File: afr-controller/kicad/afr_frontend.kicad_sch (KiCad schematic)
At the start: 37 parts, among them J1 LSU_4.9, J2 MCU_IF, Q1 VND14NV04, U1 MCP6004, U3 REF3033, U5 AD8628

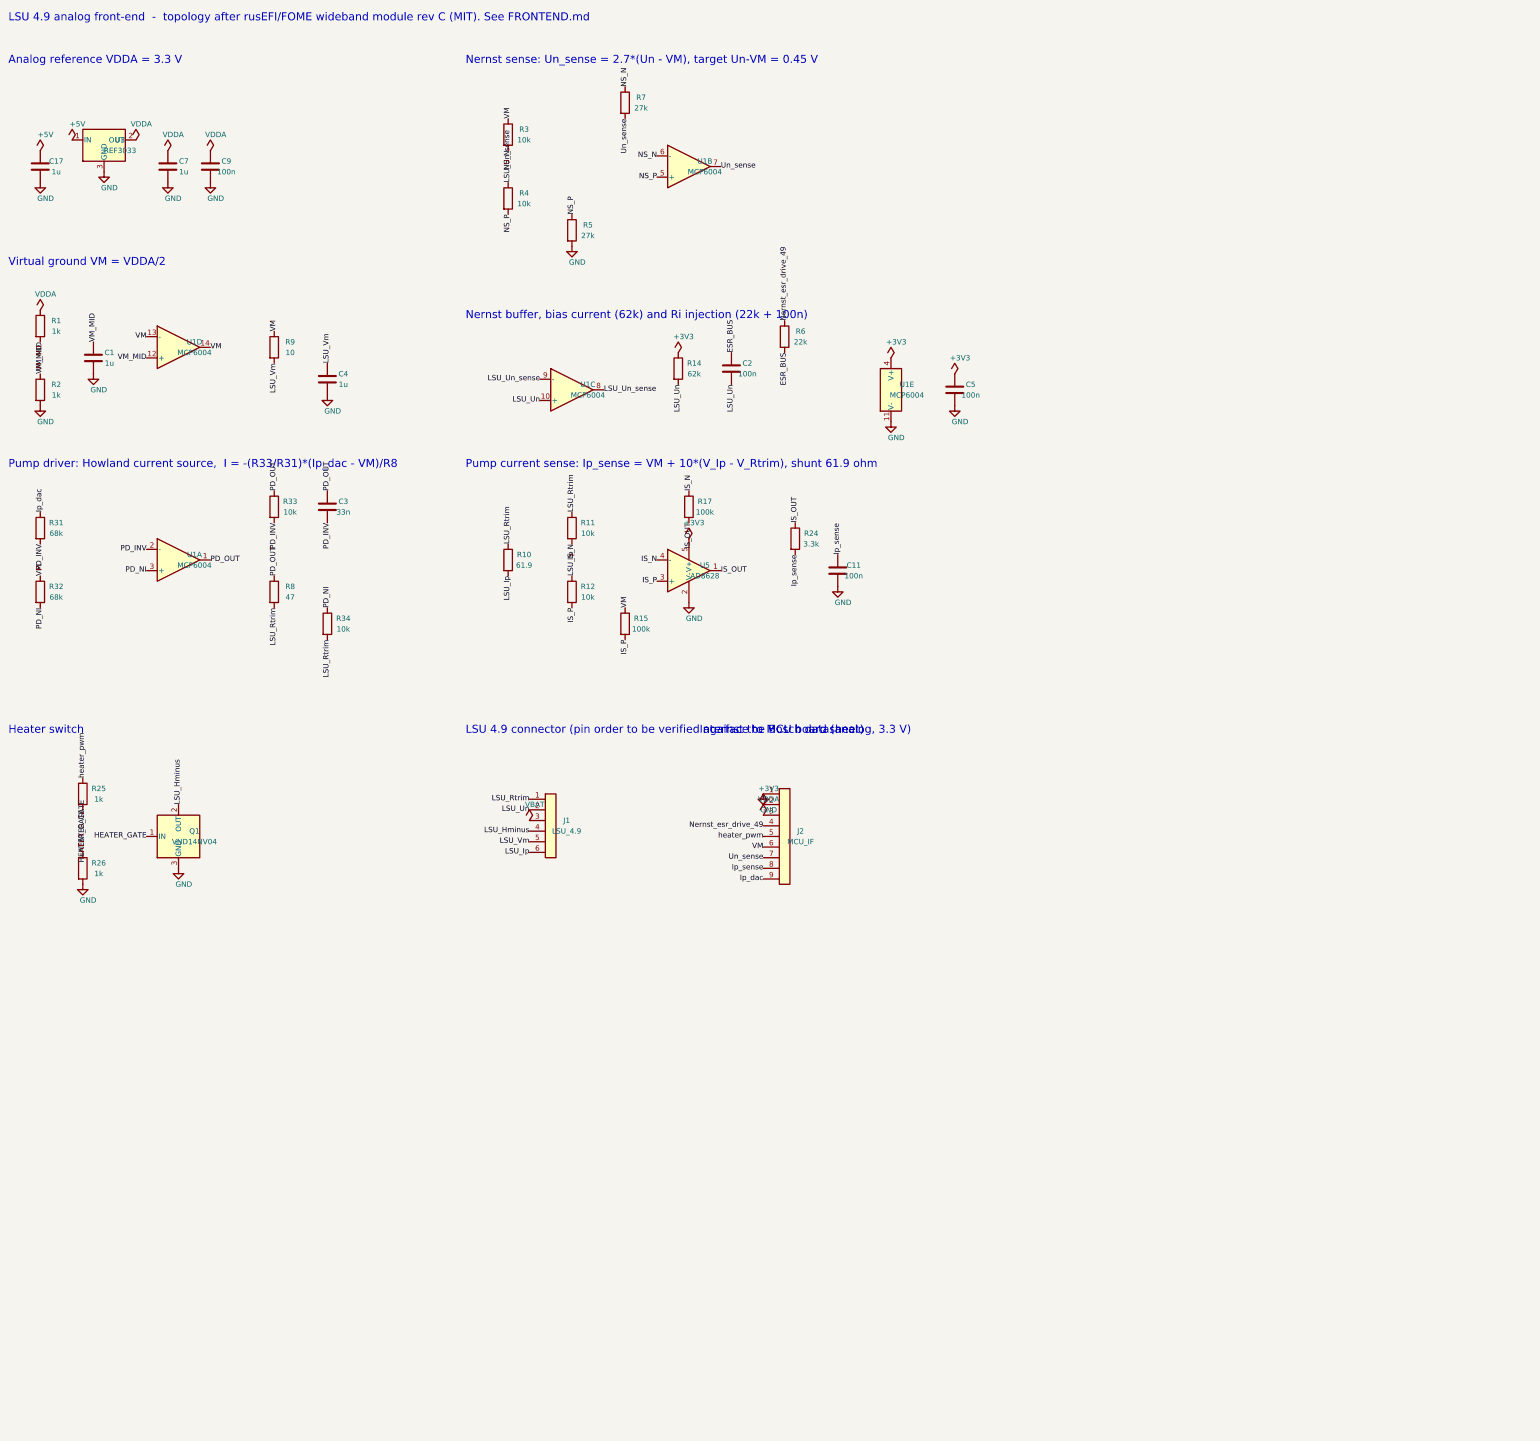
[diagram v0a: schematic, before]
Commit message: Add power, CAN and 0-5 V output to schematic generator, netlist check against kicad-cli, preview PDF
Co-Authored-By: Claude Sonnet 5.5 <noreply@anthropic.com>
Claude-Session: https://claude.ai/code/session_01RFGsein5uGNQp2jtJno8vX
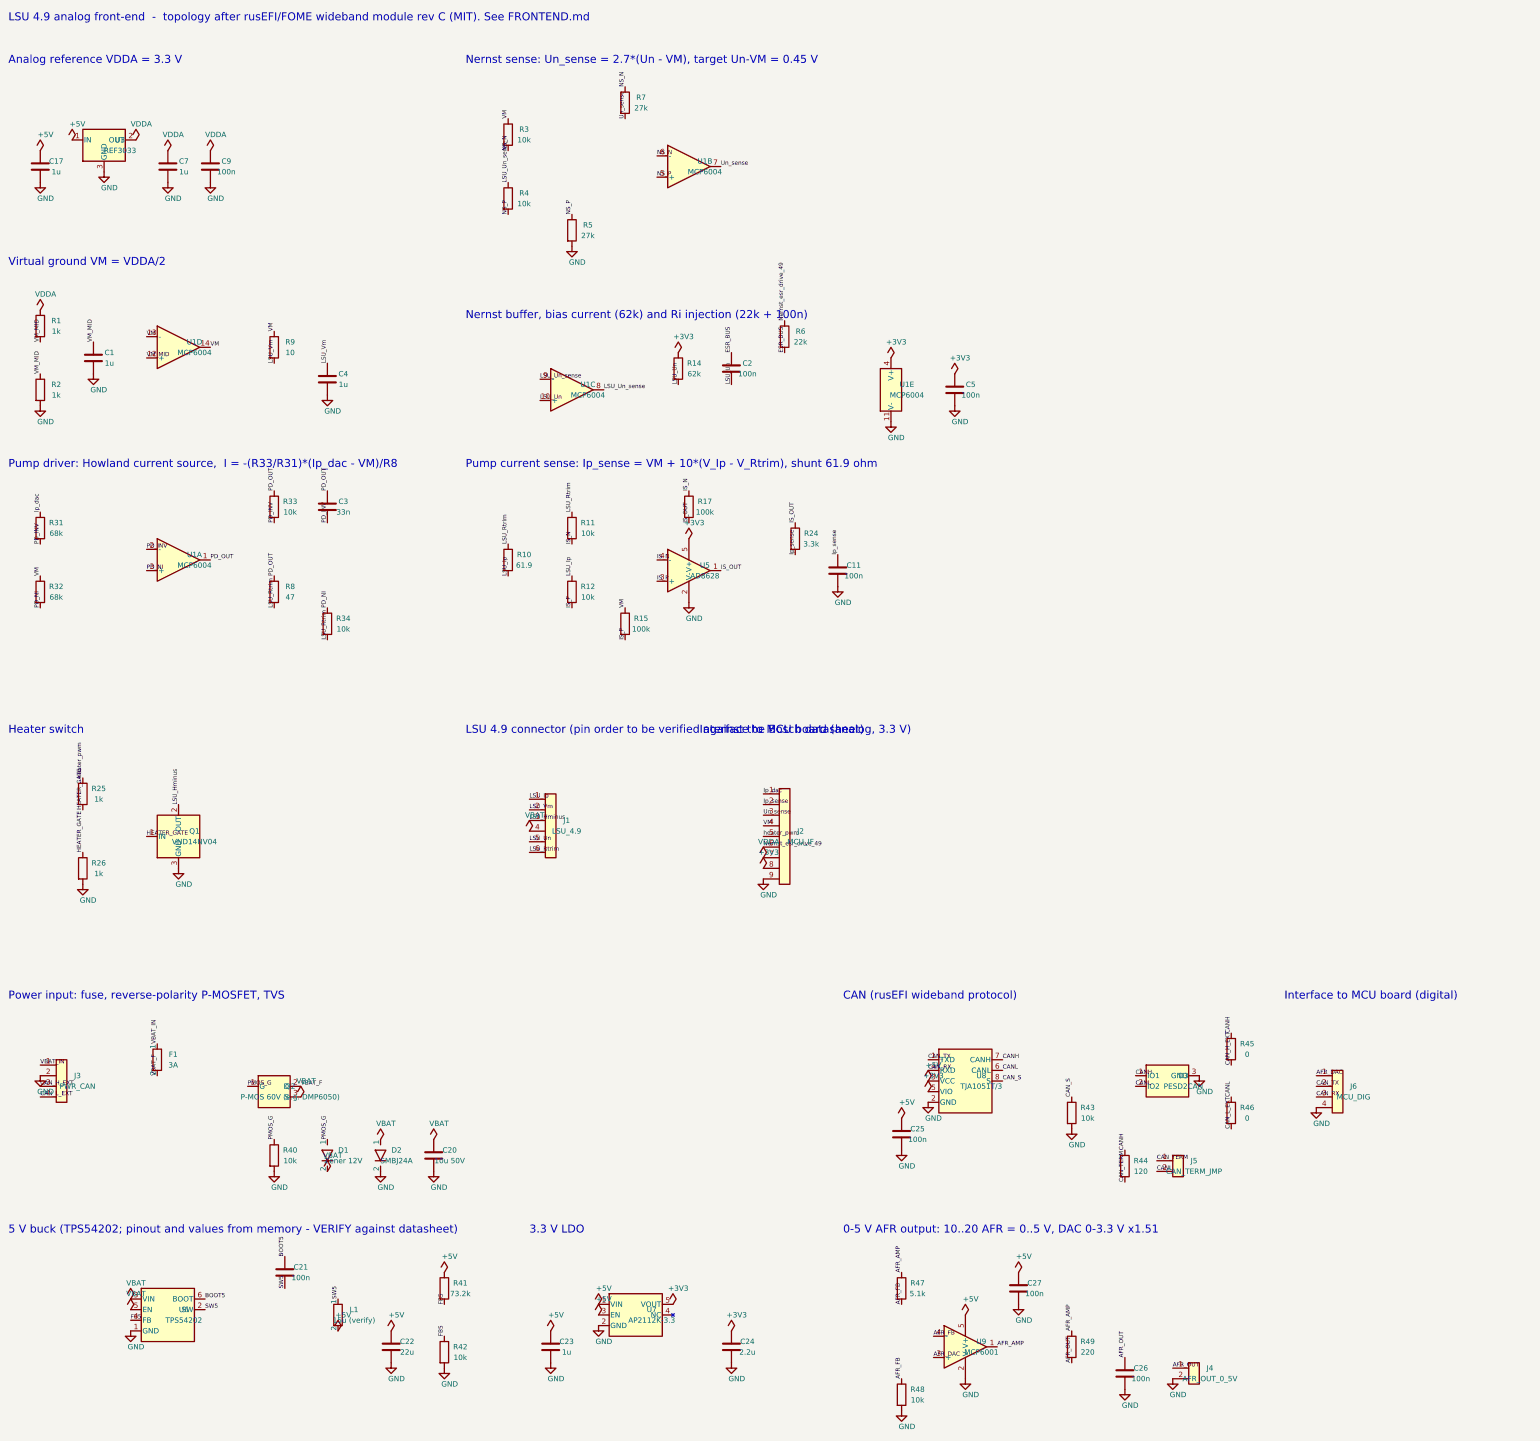
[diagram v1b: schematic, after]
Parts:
- added C20: 10u 50V, Capacitor_SMD:C_1206_3216Metric, symbol Local:C
- added C21, C25, C26, C27: 100n, Capacitor_SMD:C_0603_1608Metric, symbol Local:C
- added C22: 22u, Capacitor_SMD:C_1206_3216Metric, symbol Local:C
- added C23: 1u, Capacitor_SMD:C_0603_1608Metric, symbol Local:C
- added C24: 2.2u, Capacitor_SMD:C_0603_1608Metric, symbol Local:C
- added D1: Zener 12V, Diode_SMD:D_SOD-323, symbol Local:D
- added D2: SMBJ24A, Diode_SMD:D_SMB, symbol Local:D
- added D3: PESD2CAN, Package_TO_SOT_SMD:SOT-23, symbol Local:PESD2CAN
- added F1: 3A, Fuse:Fuse_1206_3216Metric, symbol Local:Fuse
- added J3: PWR_CAN, Connector_Molex:Molex_Micro-Fit_3.0_43650-0400, symbol Local:Conn_01x04
- added J4: AFR_OUT_0_5V, Connector_Molex:Molex_Micro-Fit_3.0_43650-0200, symbol Local:Conn_01x02
- added J5: CAN_TERM_JMP, Connector_PinHeader_2.54mm:PinHeader_1x02_P2.54mm_Vertical, symbol Local:Conn_01x02
- added J6: MCU_DIG, Connector_PinHeader_2.54mm:PinHeader_1x04_P2.54mm_Vertical, symbol Local:Conn_01x04
- added L1: 15u (verify), Inductor_SMD:L_Bourns_SRN6045, symbol Local:L
- added Q2: P-MOS 60V (e.g. DMP6050), Package_TO_SOT_SMD:SOT-23, symbol Local:Q_PMOS
- added R40, R42, R43, R48: 10k, Resistor_SMD:R_0603_1608Metric, symbol Local:R
- added R41: 73.2k, Resistor_SMD:R_0603_1608Metric, symbol Local:R
- added R44: 120, Resistor_SMD:R_0603_1608Metric, symbol Local:R
- added R45, R46: 0, Resistor_SMD:R_0603_1608Metric, symbol Local:R
- added R47: 5.1k, Resistor_SMD:R_0603_1608Metric, symbol Local:R
- added R49: 220, Resistor_SMD:R_0603_1608Metric, symbol Local:R
- added U6: TPS54202, Package_TO_SOT_SMD:SOT-23-6, symbol Local:TPS54202
- added U7: AP2112K-3.3, Package_TO_SOT_SMD:SOT-23-5, symbol Local:AP2112K-3.3
- added U8: TJA1051T/3, Package_SO:SOIC-8_3.9x4.9mm_P1.27mm, symbol Local:TJA1051T-3
- added U9: MCP6001, Package_TO_SOT_SMD:SOT-23-5, symbol Local:OPAMP5
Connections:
- net +3V3: now also J2.8 (Pin_8), C24.1, U7.5 (VOUT), U8.5 (VIO); no longer J2.2 (Pin_2)
- net +5V: now also C22.1, C23.1, C25.1, C27.1, L1.2, R41.1, U7.1 (VIN), U7.3 (EN), U8.3 (VCC), U9.5 (V+)
- net GND: now also J2.9 (Pin_9), C20.2, C22.2, C23.2, C24.2, C25.2, C26.2, C27.2, D2.2, D3.3 (GND), J3.2 (Pin_2), J4.2 (Pin_2), J6.4 (Pin_4), R40.2, R42.2, R43.2, R48.2, U6.1 (GND), U7.2 (GND), U8.2 (GND), U9.2 (V-); no longer J2.1 (Pin_1)
- net Ip_dac: now also J2.1 (Pin_1); no longer J2.9 (Pin_9)
- net Ip_sense: now also J2.2 (Pin_2); no longer J2.8 (Pin_8)
- net LSU_Hminus: now also J1.3 (Pin_3); no longer J1.4 (Pin_4)
- net LSU_Ip: now also J1.1 (Pin_1); no longer J1.6 (Pin_6)
- net LSU_Rtrim: now also J1.6 (Pin_6); no longer J1.1 (Pin_1)
- net LSU_Un: now also J1.5 (Pin_5); no longer J1.2 (Pin_2)
- net LSU_Vm: now also J1.2 (Pin_2); no longer J1.5 (Pin_5)
- net Nernst_esr_drive_49: now also J2.6 (Pin_6); no longer J2.4 (Pin_4)
- net Un_sense: now also J2.3 (Pin_3); no longer J2.7 (Pin_7)
- net VBAT: now also J1.4 (Pin_4), C20.1, D1.2, D2.1, Q2.3 (S), U6.3 (VIN), U6.5 (EN); no longer J1.3 (Pin_3)
- net VDDA: now also J2.7 (Pin_7); no longer J2.3 (Pin_3)
- net VM: now also J2.4 (Pin_4); no longer J2.6 (Pin_6)
- new net AFR_AMP: R47.1, R49.1, U9.1
- new net AFR_DAC: J6.1 (Pin_1), U9.3 (+)
- new net AFR_FB: R47.2, R48.1, U9.4 (-)
- new net AFR_OUT: C26.1, J4.1 (Pin_1), R49.2
- new net BOOT5: C21.1, U6.6 (BOOT)
- new net CANH: D3.1 (IO1), R44.1, R45.1, U8.7 (CANH)
- new net CANL: D3.2 (IO2), J5.2 (Pin_2), R46.1, U8.6 (CANL)
- new net CAN_H_EXT: J3.3 (Pin_3), R45.2
- new net CAN_L_EXT: J3.4 (Pin_4), R46.2
- new net CAN_RX: J6.3 (Pin_3), U8.4 (RXD)
- new net CAN_S: R43.1, U8.8 (S)
- new net CAN_TERM: J5.1 (Pin_1), R44.2
- new net CAN_TX: J6.2 (Pin_2), U8.1 (TXD)
- new net FB5: R41.2, R42.1, U6.4 (FB)
- new net PMOS_G: D1.1, Q2.1 (G), R40.1
- new net SW5: C21.2, L1.1, U6.2 (SW)
- new net VBAT_F: F1.2, Q2.2 (D)
- new net VBAT_IN: F1.1, J3.1 (Pin_1)
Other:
- note added: "0-5 V AFR output: 10..20 AFR = 0..5 V, DAC 0-3.3 V x1.51"
- note added: "3.3 V LDO"
- note added: "5 V buck (TPS54202; pinout and values from memory - VERIFY against datasheet)"
- note added: "CAN (rusEFI wideband protocol)"
- note added: "Interface to MCU board (digital)"
- note added: "Power input: fuse, reverse-polarity P-MOSFET, TVS"

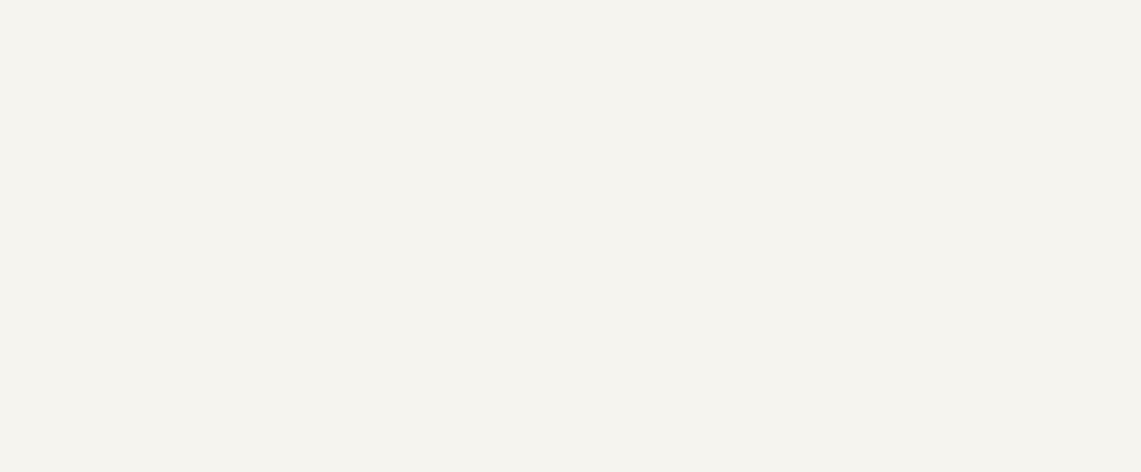
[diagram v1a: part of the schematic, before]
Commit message: Fix ERC: add PWR_FLAGs and local symbol library table
Co-Authored-By: Claude Sonnet 5.5 <noreply@anthropic.com>
Claude-Session: https://claude.ai/code/session_01RFGsein5uGNQp2jtJno8vX
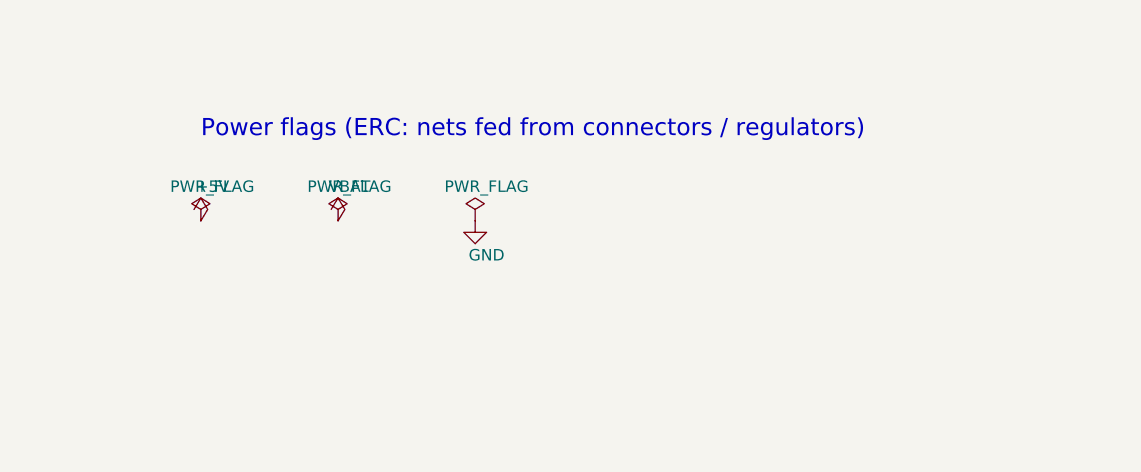
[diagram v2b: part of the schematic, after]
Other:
- note added: "Power flags (ERC: nets fed from connectors / regulators)"

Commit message: Fix footprint names, diode pin convention and P-MOS pinout; add footprint check
Co-Authored-By: Claude Sonnet 5.5 <noreply@anthropic.com>
Claude-Session: https://claude.ai/code/session_01RFGsein5uGNQp2jtJno8vX
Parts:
- J1: footprint Connector_Molex:Molex_Micro-Fit_3.0_43650-0600 -> Connector_Molex:Molex_Micro-Fit_3.0_43650-0600_1x06_P3.00mm_Horizontal
- J3: footprint Connector_Molex:Molex_Micro-Fit_3.0_43650-0400 -> Connector_Molex:Molex_Micro-Fit_3.0_43650-0400_1x04_P3.00mm_Horizontal
- J4: footprint Connector_Molex:Molex_Micro-Fit_3.0_43650-0200 -> Connector_Molex:Molex_Micro-Fit_3.0_43650-0200_1x02_P3.00mm_Horizontal
- L1: footprint Inductor_SMD:L_Bourns_SRN6045 -> Inductor_SMD:L_Bourns_SRN6045TA
- Q2: value P-MOS 60V (e.g. DMP6050) -> P-MOS >=40V >=4A, SOT-23 G1 S2 D3
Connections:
- net GND: now also D2.1 (K); no longer D2.2
- net PMOS_G: now also D1.2 (A); no longer D1.1
- net VBAT: now also D1.1 (K), D2.2 (A), Q2.2 (S); no longer D1.2, D2.1, Q2.3 (S)
- net VBAT_F: now also Q2.3 (D); no longer Q2.2 (D)

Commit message: Add MCU section (STM32G431 from stock symbol), TFT, buttons, SWD, crystal
Co-Authored-By: Claude Sonnet 5.5 <noreply@anthropic.com>
Claude-Session: https://claude.ai/code/session_01RFGsein5uGNQp2jtJno8vX
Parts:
- removed J2: MCU_IF, Connector_PinHeader_2.54mm:PinHeader_1x09_P2.54mm_Vertical, symbol Local:Conn_01x09
- removed J6: MCU_DIG, Connector_PinHeader_2.54mm:PinHeader_1x04_P2.54mm_Vertical, symbol Local:Conn_01x04
- added C30, C31, C32, C35, C36, C37: 100n, Capacitor_SMD:C_0603_1608Metric, symbol Local:C
- added C33: 4.7u, Capacitor_SMD:C_0603_1608Metric, symbol Local:C
- added C34, C40: 1u, Capacitor_SMD:C_0603_1608Metric, symbol Local:C
- added C38, C39: 15p, Capacitor_SMD:C_0603_1608Metric, symbol Local:C
- added J7: TFT_ST7789, Connector_PinHeader_2.54mm:PinHeader_1x08_P2.54mm_Vertical, symbol Local:Conn_01x08
- added J8: BUTTONS, Connector_PinHeader_2.54mm:PinHeader_1x04_P2.54mm_Vertical, symbol Local:Conn_01x04
- added J9: SWD, Connector_PinHeader_2.54mm:PinHeader_1x05_P2.54mm_Vertical, symbol Local:Conn_01x05
- added R60: 100k, Resistor_SMD:R_0603_1608Metric, symbol Local:R
- added R61, R62: 10k, Resistor_SMD:R_0603_1608Metric, symbol Local:R
- added R63: 100, Resistor_SMD:R_0603_1608Metric, symbol Local:R
- added U2: STM32G431CBT6, Package_QFP:LQFP-48_7x7mm_P0.5mm, symbol Local:STM32G431CBTx
- added Y1: 8 MHz, Crystal:Crystal_SMD_5032-2Pin_5.0x3.2mm, symbol Local:Crystal
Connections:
- net +3V3: now also C30.1, C31.1, C32.1, C33.1, C36.1, J7.2 (Pin_2), J9.1 (Pin_1), U2.1 (VBAT), U2.24 (VDD), U2.36 (VDD), U2.48 (VDD)
- net AFR_DAC: now also U2.13 (PA5)
- net CAN_RX: now also U2.33 (PA11)
- net CAN_TX: now also U2.34 (PA12)
- net GND: now also C30.2, C31.2, C32.2, C33.2, C34.2, C35.2, C36.2, C37.2, C38.2, C39.2, C40.2, J7.1 (Pin_1), J8.4 (Pin_4), J9.5 (Pin_5), R61.2, R62.2, U2.19 (VSSA), U2.23 (VSS), U2.35 (VSS), U2.47 (VSS)
- net Ip_dac: now also U2.12 (PA4)
- net Ip_sense: now also U2.8 (PA0)
- net Nernst_esr_drive_49: now also U2.16 (PB0)
- net Un_sense: now also U2.9 (PA1)
- net VBAT: now also R60.1
- net VDDA: now also C34.1, C35.1, U2.20 (VREF+), U2.21 (VDDA)
- net VM: now also U2.10 (PA2)
- net heater_pwm: now also U2.30 (PA8)
- new net BOOT0: R62.1, U2.45 (PB8)
- new net BTN1: J8.1 (Pin_1), U2.42 (PB5)
- new net BTN2: J8.2 (Pin_2), U2.43 (PB6)
- new net BTN3: J8.3 (Pin_3), U2.44 (PB7)
- new net NRST: C37.1, J9.4 (Pin_4), U2.7 (PG10)
- new net OSC_IN: C38.1, U2.5 (PF0), Y1.1
- new net OSC_OUT: C39.1, U2.6 (PF1), Y1.2
- new net SPI_MOSI: J7.4 (Pin_4), U2.29 (PB15)
- new net SPI_SCK: J7.3 (Pin_3), U2.27 (PB13)
- new net SWCLK: J9.3 (Pin_3), U2.38 (PA14)
- new net SWDIO: J9.2 (Pin_2), U2.37 (PA13)
- new net TFT_BL: J7.8 (Pin_8), R63.2
- new net TFT_BL_MCU: R63.1, U2.41 (PB4)
- new net TFT_CS: J7.7 (Pin_7), U2.26 (PB12)
- new net TFT_DC: J7.6 (Pin_6), U2.22 (PB10)
- new net TFT_RES: J7.5 (Pin_5), U2.25 (PB11)
- new net VBAT_SENSE: C40.1, R60.2, R61.1, U2.11 (PA3)
- no-connect marks 0 -> 13
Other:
- note added: "MCU: STM32G431CBT6 (pin functions from memory - verify AF in CubeMX)"
- note added: "TFT module (ST7789 SPI), buttons, SWD"
- note removed: "Interface to MCU board (analog, 3.3 V)"
- note removed: "Interface to MCU board (digital)"
